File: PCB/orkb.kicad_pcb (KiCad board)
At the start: 2 copper layers, 148.5 x 113.3 mm, 114 parts, among them J1 USB_C_Receptacle_USB2.0, P1 OLED, SW1 MXHS, SW10 MXHS, SW11 MXHS, SW12 MXHS, SW13 MXHS, SW14 MXHS, SW15 MXHS, SW16 MXHS, SW17 MXHS, SW18 MXHS, SW19 MXHS, SW2 MXHS, SW20 MXHS, SW21 MXHS, SW22 MXHS, SW23 MXHS, SW24 MSK12C02, SW25 MSK12C02, SW3 MXHS, SW4 MXHS, SW5 MXHS, SW6 MXHS, SW7 MXHS, SW8 MXHS, SW9 MXHS, U1 ProMicro, U2 SRV05-4, U3 SRV05-4

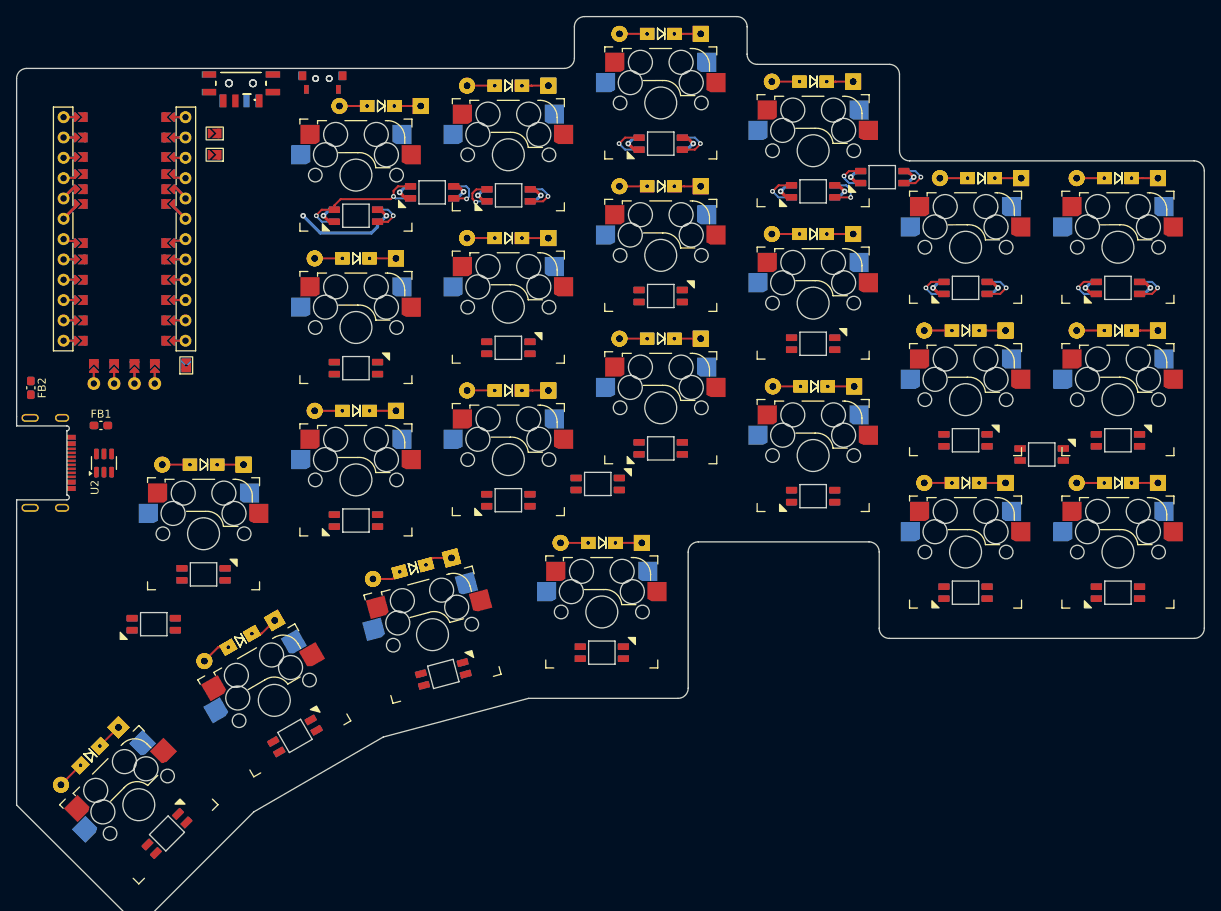
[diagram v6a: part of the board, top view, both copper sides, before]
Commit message: Added all LED reversible connections
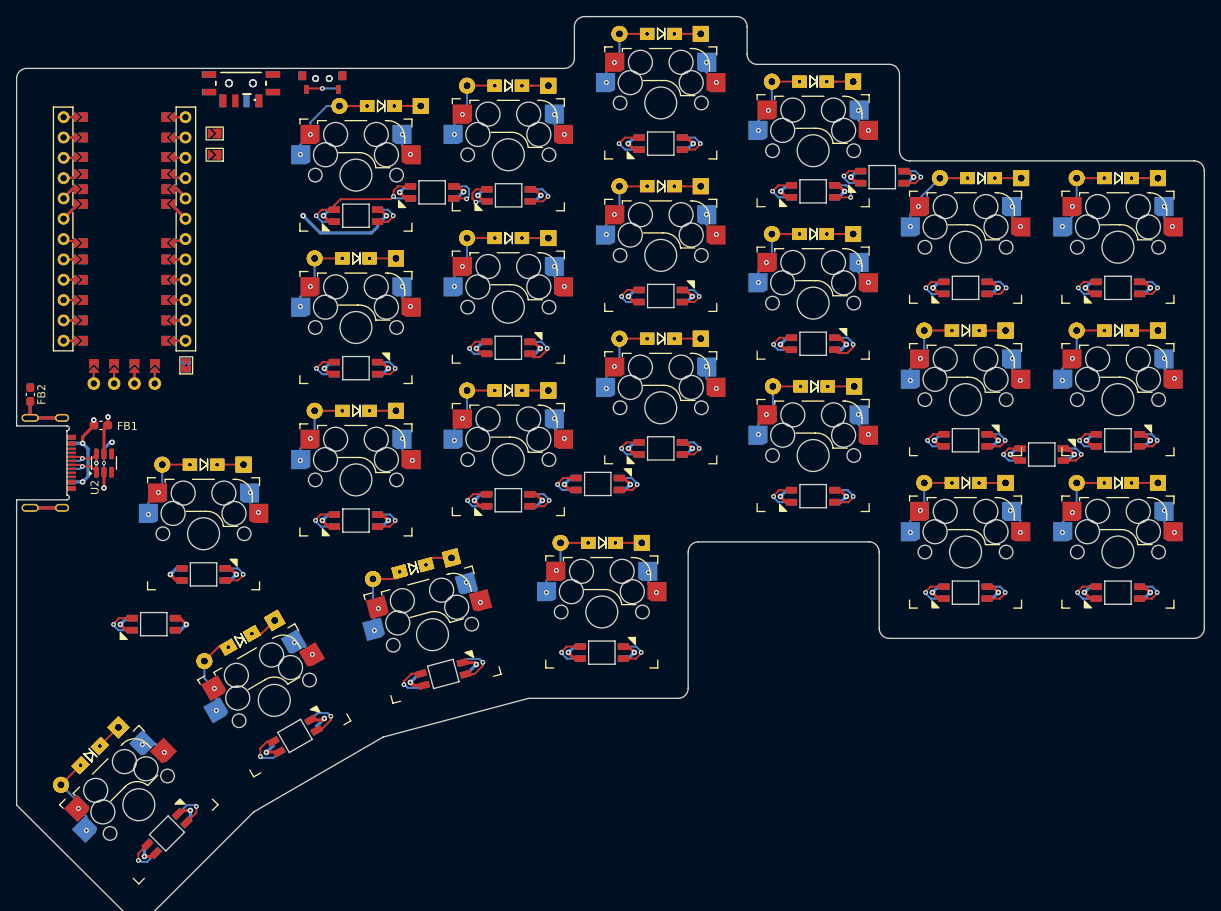
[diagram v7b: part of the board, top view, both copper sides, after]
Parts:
- SW23: moved to B.Cu
- moved FB2 0.83 mm to (67.0, 88.0)
- moved FB4 0.83 mm to (67.0, 88.0)
- turned SW23 to 180 degrees
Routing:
- net GND: track 26.1 -> 99.1 mm, vias 8 -> 30
- net /PWR_KEY: track 30.4 -> 87.4 mm, vias 7 -> 24
- net Net-(J1-SHIELD): track 0.00 -> 20.2 mm
- net col0: track 0.00 -> 15.2 mm, vias 0 -> 10
- net DATA: track 0.00 -> 14.2 mm, vias 0 -> 3
- net col2: track 0.00 -> 12.5 mm, vias 0 -> 8
- net col3: track 0.00 -> 12.0 mm, vias 0 -> 8
- net col1: track 0.00 -> 11.9 mm, vias 0 -> 8
- net Net-(LED21-DIN): track 0.00 -> 11.5 mm, vias 0 -> 2
- net /VCC_LINK: track 0.00 -> 11.5 mm, vias 0 -> 3
- net Net-(LED22-DIN): track 0.00 -> 11.3 mm, vias 0 -> 2
- net Net-(LED20-DIN): track 0.00 -> 11.1 mm, vias 0 -> 2
- net Net-(LED27-DOUT): track 0.00 -> 10.8 mm, vias 0 -> 2
- net Net-(LED14-DOUT): track 0.00 -> 10.7 mm, vias 0 -> 2
- net Net-(LED10-DIN): track 0.00 -> 10.7 mm, vias 0 -> 2
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
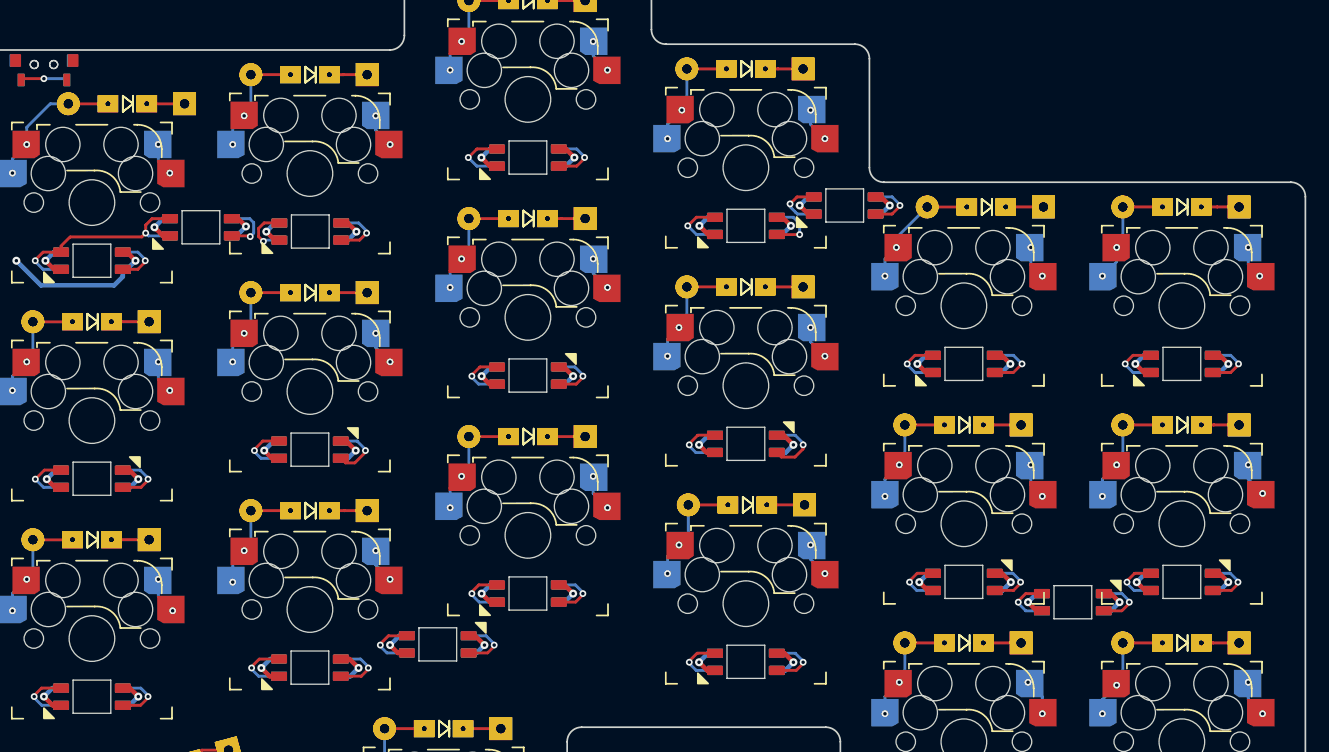
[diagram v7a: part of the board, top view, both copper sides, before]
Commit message: Initial column routing
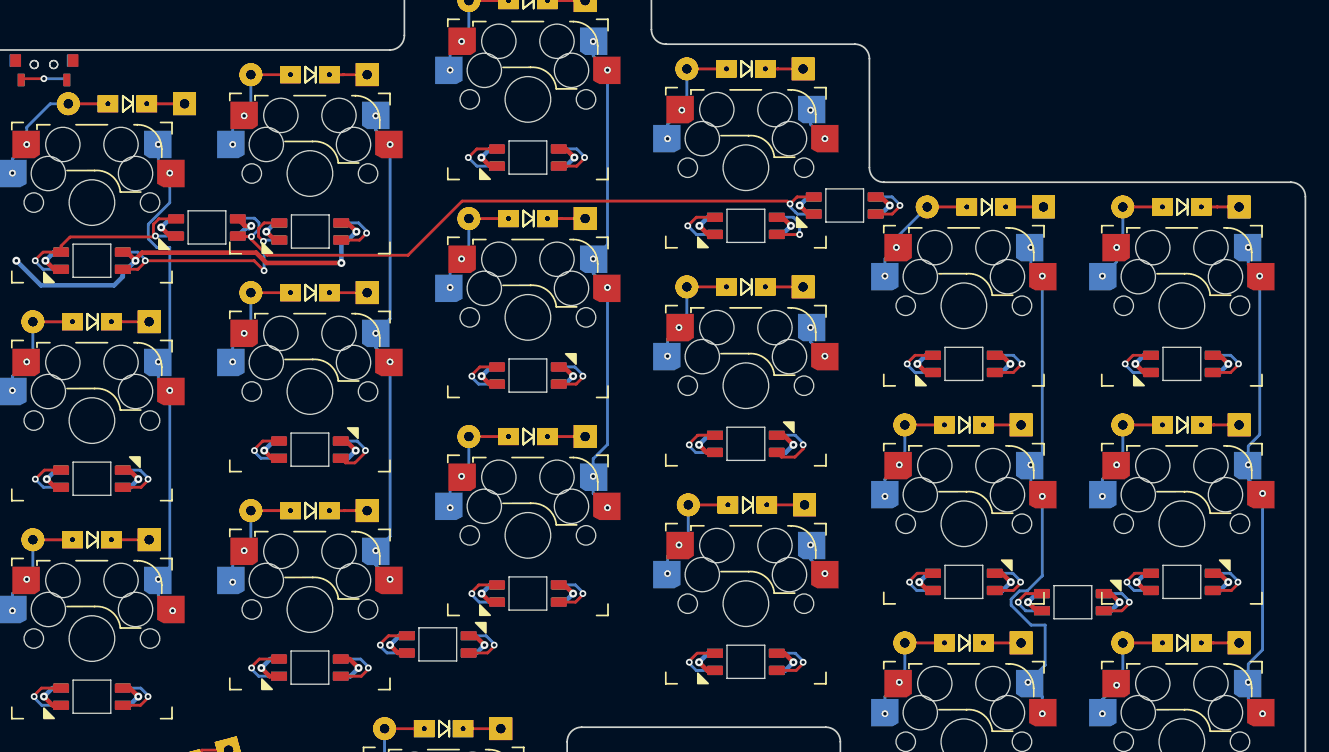
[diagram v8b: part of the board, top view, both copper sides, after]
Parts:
- moved LED24 0.53 mm to (117.8, 62.8)
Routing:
- net Net-(LED24-DOUT): track 9.96 -> 60.0 mm
- net col4: track 9.35 -> 46.6 mm
- net col0: track 15.2 -> 51.2 mm
- net col2: track 12.5 -> 46.6 mm
- net col1: track 11.9 -> 46.0 mm
- net col5: track 9.20 -> 43.1 mm
- net /PWR_KEY: track 87.4 -> 108.3 mm, vias 24 -> 25
- net Net-(LED1-DOUT): track 9.43 -> 22.9 mm, vias 2 -> 3
- net LED: track 18.9 -> 19.4 mm
